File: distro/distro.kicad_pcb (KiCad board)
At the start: 2 copper layers, 59.1 x 76.8 mm, 19 parts, among them K1 CONN_3, K2 CONN_3, K3 CONN_3, K4 CONN_3, P4 CONN_2, P5 CONN_2, P6 CONN_2, P7 CONN_2

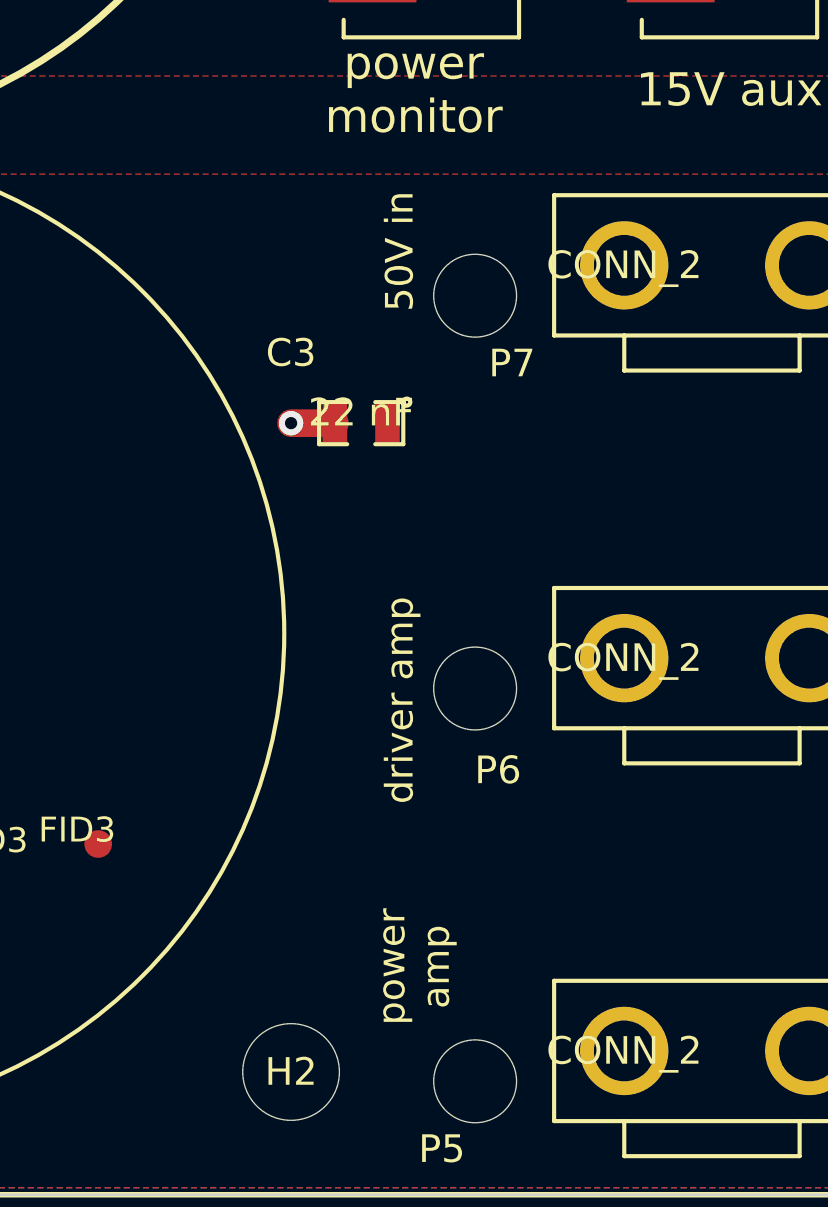
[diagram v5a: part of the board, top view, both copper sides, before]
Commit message: added fields for manufacturer/distributor part number to schematic
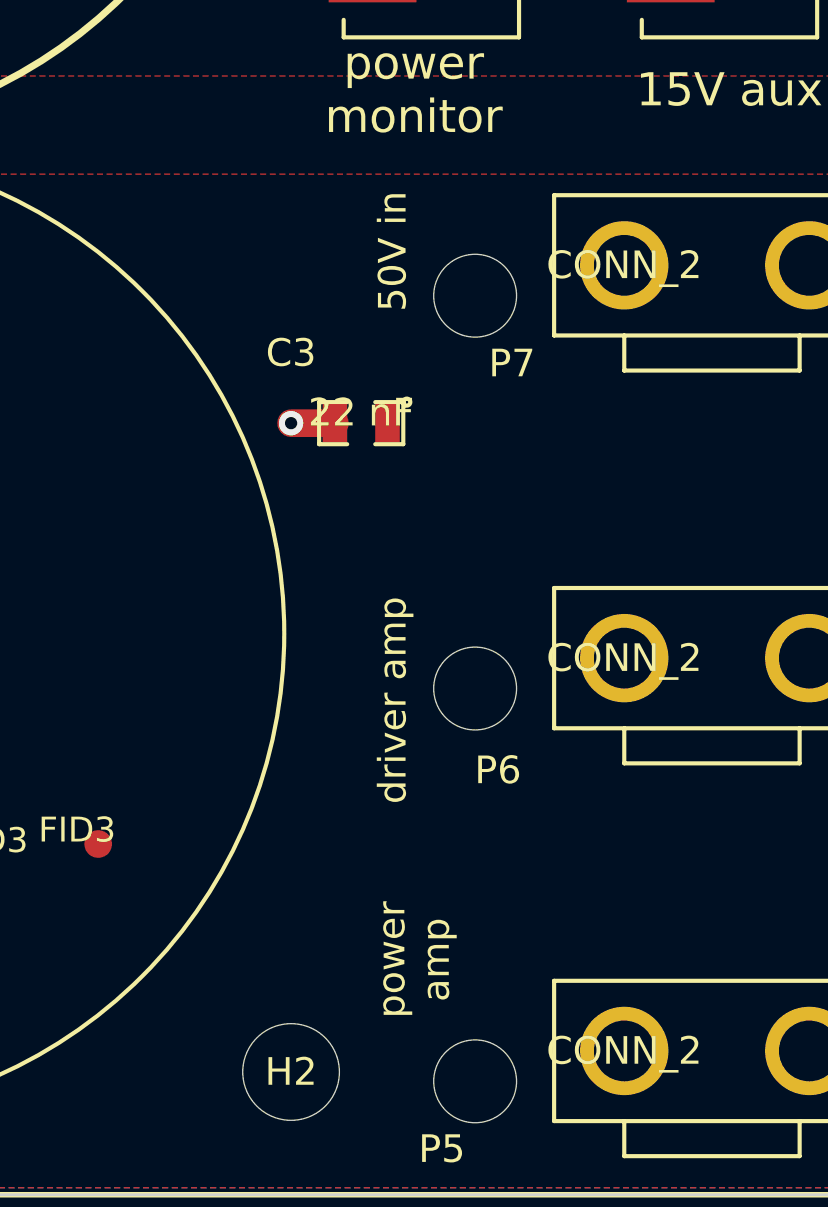
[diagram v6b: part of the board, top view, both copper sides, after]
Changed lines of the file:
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@@
     (links 24)
     (no_connects 0)
-    (area 76.784999 61.862499 135.940001 138.797501)
+    (area 74.829572 61.812499 137.247572 140.38276)
     (thickness 1.6)
     (drawings 18)
@@
   (page A3)
   (layers
-    (15 F.Cu signal)
-    (0 B.Cu signal)
+    (15 F.Cu signal hide)
+    (0 B.Cu signal hide)
     (16 B.Adhes user)
     (17 F.Adhes user)
@@
     (effects (font (size 1.5 1.5) (thickness 0.3)) (justify mirror))
   )
-  (gr_text "50V in" (at 117.602 104.5845 90) (layer F.SilkS)
+  (gr_text "50V in" (at 117.348 104.5845 90) (layer F.SilkS)
     (effects (font (size 1 1) (thickness 0.25)))
   )
-  (gr_text "driver amp" (at 117.602 120.8405 90) (layer F.SilkS)
+  (gr_text "driver amp" (at 117.348 120.8405 90) (layer F.SilkS)
     (effects (font (size 1 1) (thickness 0.25)))
   )
-  (gr_text "power\namp" (at 118.11 130.4925 90) (layer F.SilkS)
+  (gr_text "power\namp" (at 118.11 130.2385 90) (layer F.SilkS)
     (effects (font (size 1 1) (thickness 0.25)))
   )

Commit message: added dfm changes from fab, I think
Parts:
- added D1: LED, LEDs:LED-0805, F.Cu at (112.3, 98.0)
- added D2: LED, LEDs:LED-0805, F.Cu at (112.3, 102.3)
- added R1: 10k, Resistors_SMD:R_0805, F.Cu at (109.7, 98.2)
- added R2: 100k, Resistors_SMD:R_0805, F.Cu at (109.7, 102.0)
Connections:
- K1 pad 1: (no net) -> Net-(K1-Pad1)
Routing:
- net GND: track 22.3 -> 25.4 mm, vias 9 -> 11
- net Net-(D2-Pad1): track 0.00 -> 2.95 mm
- net Net-(D1-Pad1): track 0.00 -> 2.79 mm
